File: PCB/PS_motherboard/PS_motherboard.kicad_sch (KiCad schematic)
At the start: 14 parts, among them J1 Screw_Terminal_01x06, J2 Conn_01x06_Socket, J3 Conn_01x04_Socket, J4 Conn_01x05_Pin, J5 GPIO_CONNECTOR, SW1 SW_Push

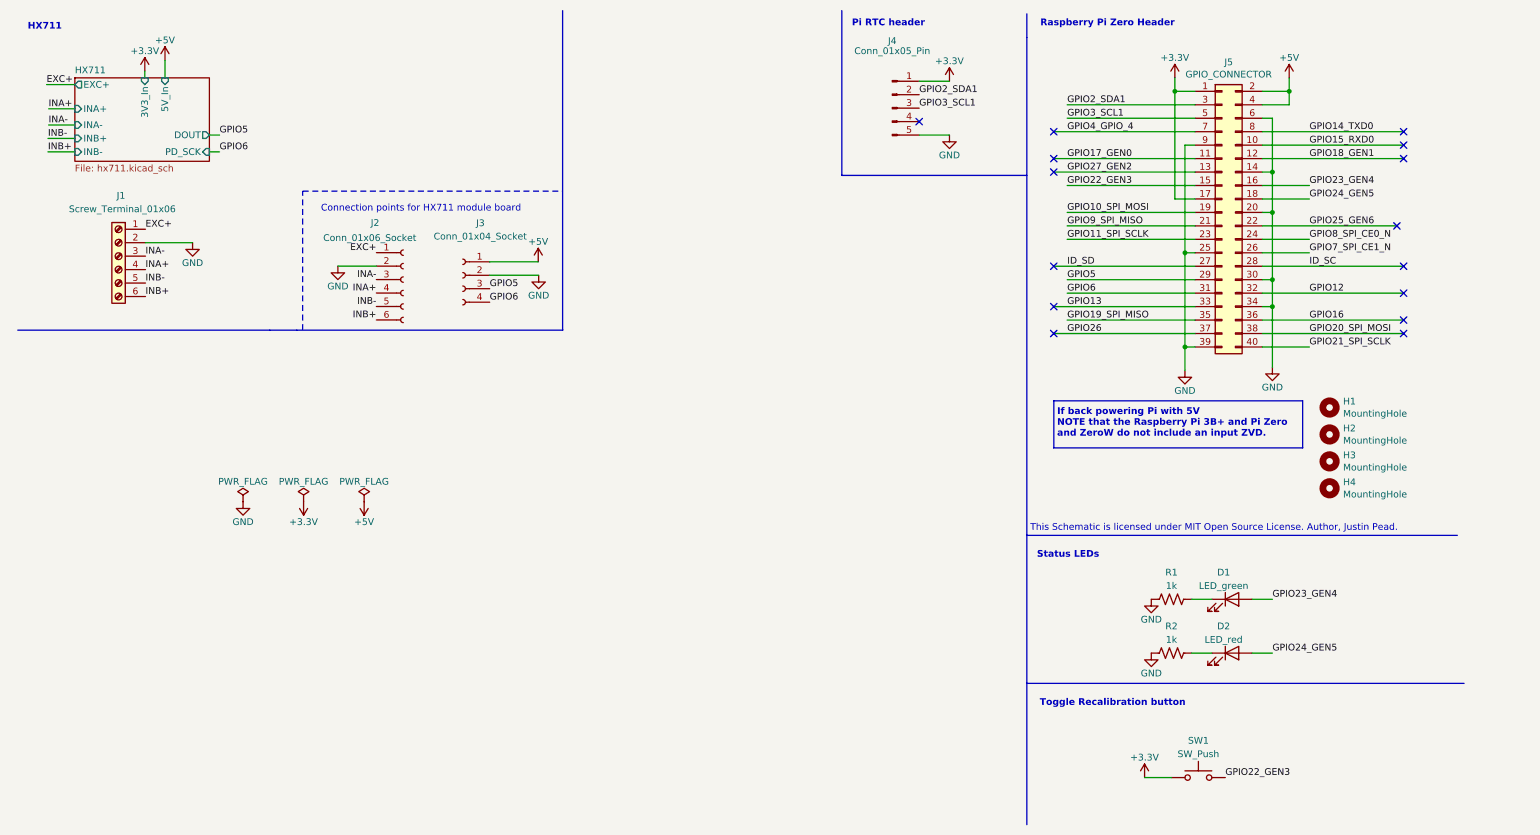
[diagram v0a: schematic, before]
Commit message: Updated LCSC part numbers and footprints for all parts EXCEPT PB and Screw Terminals (added comments why not)
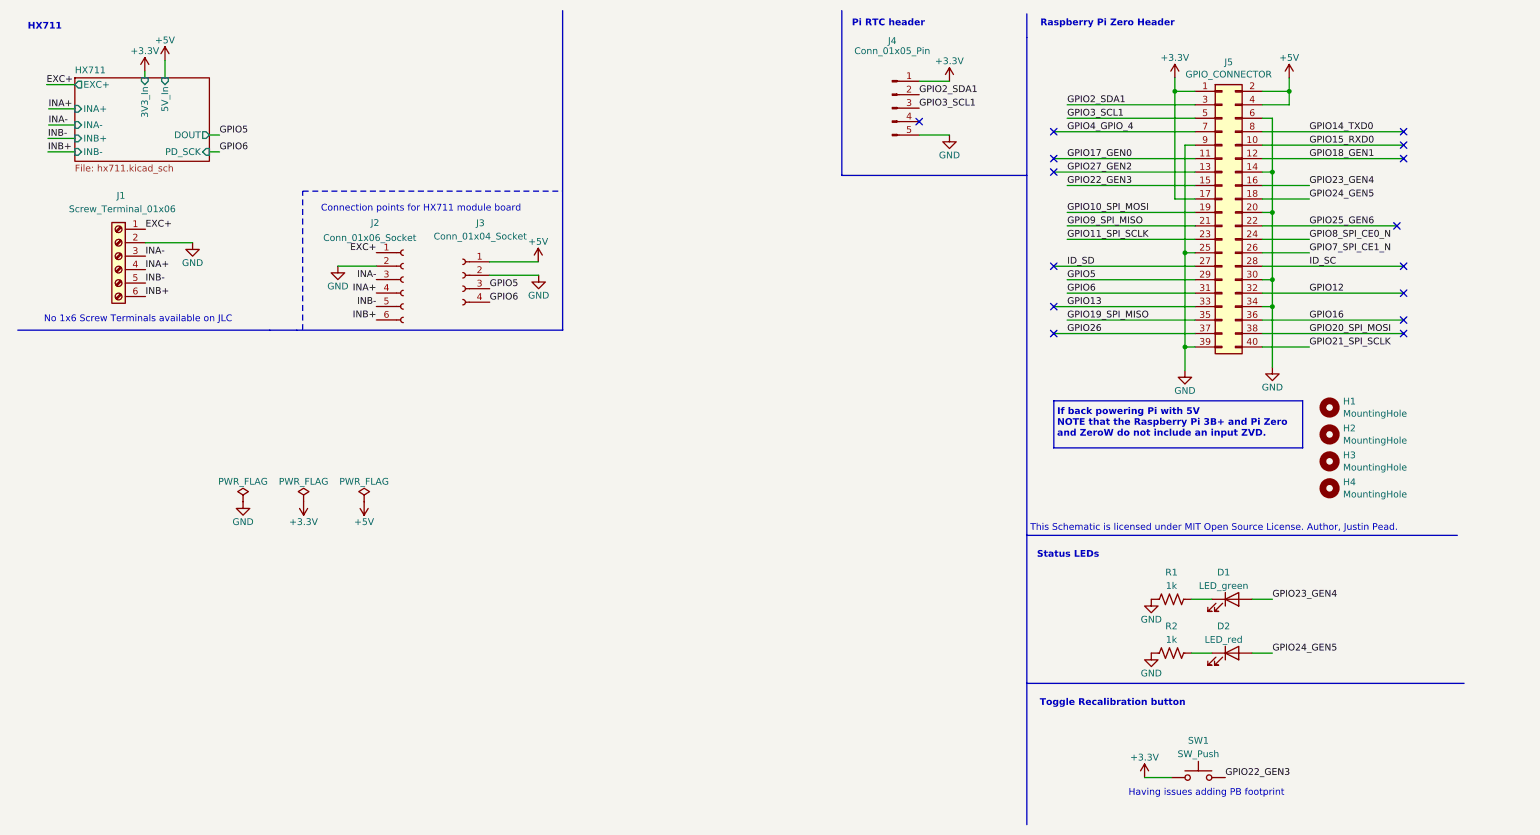
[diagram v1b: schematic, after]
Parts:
- D1: footprint (none) -> LED_SMD:LED_0603_1608Metric; Extended (none) -> 1; LCSC (none) -> C5123548
- D2: footprint (none) -> LED_SMD:LED_0603_1608Metric; Extended (none) -> 1; LCSC (none) -> C7371906
- J2, J3, J4: Populate (none) -> 0
- R1, R2: footprint (none) -> Resistor_SMD:R_0603_1608Metric; Extended (none) -> 0; LCSC (none) -> C21190
- SW1: Extended (none) -> 1; LCSC (none) -> C470427
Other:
- note added: "Having issues adding PB footprint"
- note added: "No 1x6 Screw Terminals available on JLC"

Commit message: Update footprints
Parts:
- J1: Extended (none) -> 1; LCSC (none) -> https://jlcpcb.com/parts/2nd/Connectors/Screw_Terminal_3902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
- SW1: LCSC C470427 -> C2848967
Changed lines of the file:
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@@
+			)
+		)
+		(property "Extended" "1"
+			(at 31.115 58.42 0)
+			(effects
+				(font
+					(size 1.27 1.27)
+				)
+				(hide yes)
+			)
+		)
+		(property "LCSC" "https://jlcpcb.com/parts/2nd/Connectors/Screw_Terminal_3902?searchTxt=Phoenix%20contact"
+			(at 31.115 58.42 0)
+			(effects
+				(font
+					(size 1.27 1.27)
+				)
+				(hide yes)
 			)
 		)
@@
 			)
 		)
-		(property "Datasheet" "https://wmsc.lcsc.com/wmsc/upload/file/pdf/v2/lcsc/2005150044_ALPSALPINE-SKRPASE010_C470427.pdf"
+		(property "Datasheet" "https://wmsc.lcsc.com/wmsc/upload/file/pdf/v2/lcsc/2108142330_G-Switch-GT-TCA84B-H015-L10_C2848967.pdf"
 			(at 234.95 151.765 0)
 			(effects
@@
 			)
 		)
-		(property "LCSC" "C470427"
+		(property "LCSC" "C2848967"
 			(at 234.95 156.845 0)
 			(effects
